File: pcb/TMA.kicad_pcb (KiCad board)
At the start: 2 copper layers, 6 parts, among them U1 BMP280, U2 BMI160, U3 STM32F030C6Tx

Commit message: Pick components.
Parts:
- added C4: 4u7, Capacitor_SMD:C_0402_1005Metric, F.Cu at (116.0, 84.4)
- added C5: 100nF, Capacitor_SMD:C_0402_1005Metric, F.Cu at (111.2, 88.7)
- added C6: 4u7, Capacitor_SMD:C_0402_1005Metric, F.Cu at (114.1, 86.4)
- added C7: 100nF, Capacitor_SMD:C_0402_1005Metric, F.Cu at (110.5, 90.7)
- added D1: D_Schottky, Diode_SMD:D_0402_1005Metric, F.Cu at (82.8, 91.9)
- added D3: BLUE, LED_SMD:LED_0402_1005Metric, F.Cu at (103.4, 75.9)
- added D4: RED, LED_SMD:LED_0402_1005Metric, F.Cu at (103.4, 80.0)
- added J1: Conn_01x02, Connector_JST:JST_PH_B2B-PH-K_1x02_P2.00mm_Vertical, F.Cu at (88.1, 64.5)
- added J2: Conn_01x06, Connector_JST:JST_PH_B6B-PH-K_1x06_P2.00mm_Vertical, F.Cu at (93.5, 63.5)
- added R1: 5k, Resistor_SMD:R_0402_1005Metric, F.Cu at (108.3, 86.7)
- added R2: 10k, Resistor_SMD:R_0402_1005Metric, F.Cu at (106.4, 75.9)
- added R3: 10k, Resistor_SMD:R_0402_1005Metric, F.Cu at (106.4, 80.0)
- added R4: 10k, Resistor_SMD:R_0402_1005Metric, F.Cu at (108.3, 88.7)
- added R5: 10k, Resistor_SMD:R_0402_1005Metric, F.Cu at (122.9, 82.0)
- added SW1: SW_SPDT, Button_Switch_SMD:SW_SPDT_PCM12, F.Cu at (86.4, 74.4)
- added U4: MIC5504-3.3YM5, Package_TO_SOT_SMD:SOT-23-5, F.Cu at (77.7, 93.0)
- U3: value STM32F030C6Tx -> ATtiny1614-SS; footprint Package_QFP:LQFP-48_7x7mm_P0.5mm -> Package_SO:SOIC-14_3.9x8.7mm_P1.27mm
- moved U1 37.4 mm to (107.4, 69.6)
- moved U3 36.9 mm to (96.0, 74.7)
- moved C3 31.0 mm to (107.7, 90.7)
- moved C2 30.3 mm to (122.7, 70.1)
- moved U2 30.0 mm to (114.0, 69.8)
- moved C1 24.6 mm to (114.1, 88.4)
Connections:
- U3 pad 10: Net-(U3-Pad10) -> UPDI
- U3 pad 11: Net-(U3-Pad11) -> SDA
- U3 pad 12: Net-(U3-Pad12) -> SCL
- U3 pad 14: Net-(U3-Pad14) -> GND
- U3 pad 6: Net-(U3-Pad6) -> MODE
- U3 pad 7: GND -> Net-(U3-Pad7)
- U3 pad 8: GND -> LED1
- U3 pad 9: +3V3 -> LED0
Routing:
- net GND: track 0.00 -> 4.32 mm
- net Net-(D3-Pad1): track 0.00 -> 2.08 mm
- net Net-(D4-Pad1): track 0.00 -> 2.05 mm

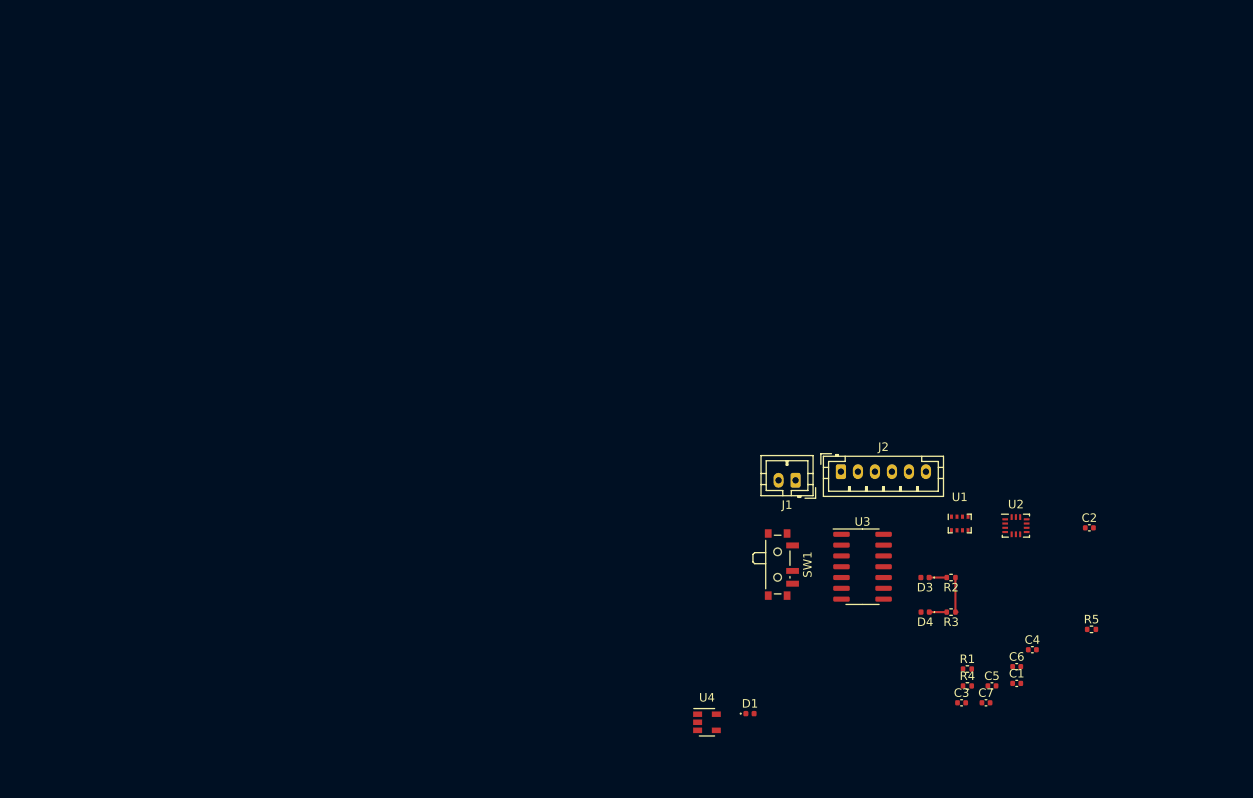
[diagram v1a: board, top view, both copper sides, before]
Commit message: Simplify, add voltage to extension.
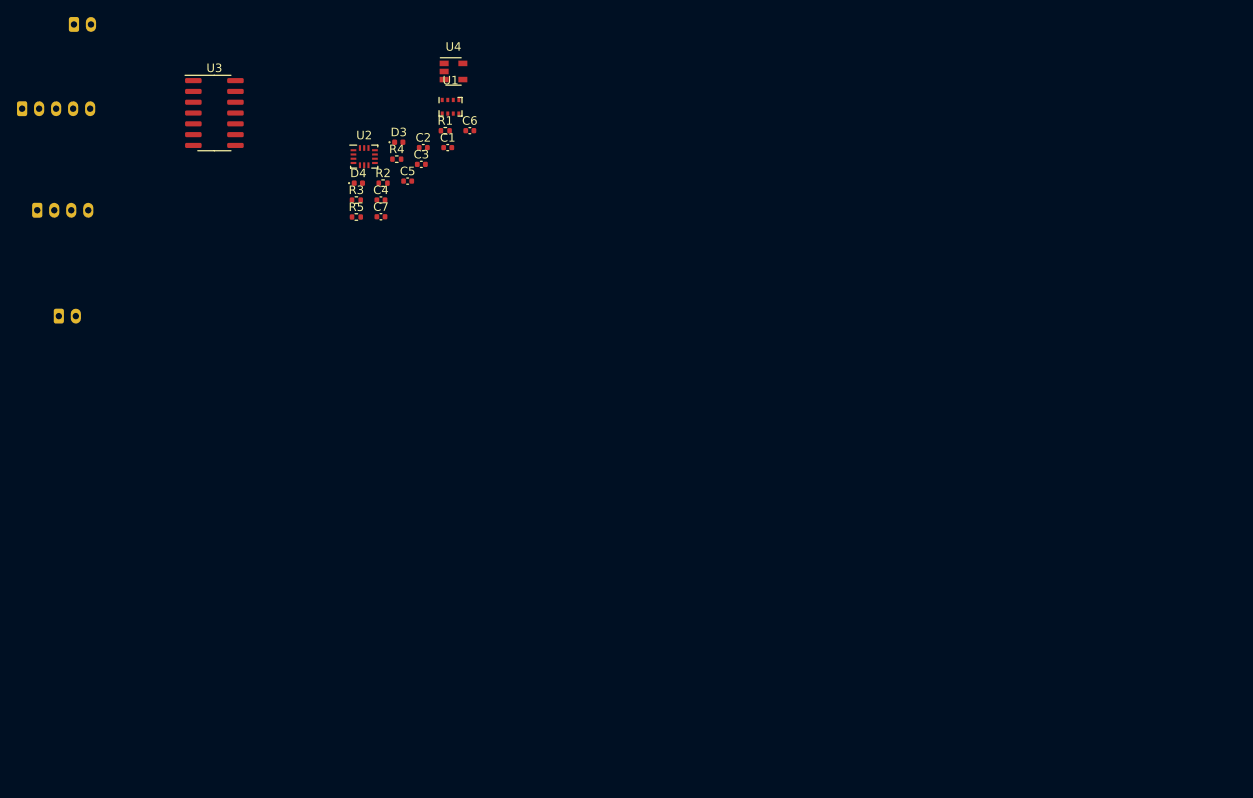
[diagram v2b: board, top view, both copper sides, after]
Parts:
- removed D1: D_Schottky, Diode_SMD:D_0402_1005Metric
- removed SW1: SW_SPDT, Button_Switch_SMD:SW_SPDT_PCM12
- added J3: Conn_01x04, Connector_JST:JST_PH_S4B-PH-K_1x04_P2.00mm_Horizontal, B.Cu at (-1.02, 32.8)
- added J4: Conn_01x02, Connector_JST:JST_PH_S2B-PH-K_1x02_P2.00mm_Horizontal, B.Cu at (3.30, 10.9)
- J1: footprint Connector_JST:JST_PH_B2B-PH-K_1x02_P2.00mm_Vertical -> Connector_JST:JST_PH_S2B-PH-K_1x02_P2.00mm_Horizontal; moved to B.Cu
- J2: value Conn_01x06 -> Conn_01x05; footprint Connector_JST:JST_PH_B6B-PH-K_1x06_P2.00mm_Vertical -> Connector_JST:JST_PH_S5B-PH-K_1x05_P2.00mm_Horizontal; moved to B.Cu
- R1: value 5k -> 10k
- R2, R3: value 10k -> 100
- R4, R5: value 10k -> 4k7
- moved J2 105.3 mm to (-2.79, 20.8)
- moved R5 99.1 mm to (36.5, 33.6)
- moved C4 93.1 mm to (39.4, 31.6)
- moved U3 93.0 mm to (19.8, 21.3)
- moved C1 91.9 mm to (47.2, 25.4)
- moved R4 91.3 mm to (41.3, 26.8)
- moved C7 91.2 mm to (39.4, 33.5)
- moved C5 90.8 mm to (42.5, 29.3)
- moved C2 90.2 mm to (44.4, 25.4)
- moved C6 90.0 mm to (49.8, 23.4)
- moved C3 89.7 mm to (44.1, 27.4)
- moved J1 88.7 mm to (1.52, 45.2), turned to 0 degrees
- moved R1 88.2 mm to (47.0, 23.4)
- moved U2 88.1 mm to (37.4, 26.5)
- moved R3 85.1 mm to (36.5, 31.6), turned to 0 degrees
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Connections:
- J2 pad 1: SCL -> TXD
- J2 pad 2: SDA -> RXD
- J2 pad 3: GND -> UPDI
- J2 pad 4: UPDI -> GND
- J2 pad 5: Net-(J2-Pad5) -> +3V3
- R1 pad 1: UPDI -> GND
- R1 pad 2: Net-(J2-Pad5) -> MODE
- U3 pad 5: Net-(U3-Pad5) -> MODE
- U3 pad 6: MODE -> RXD
- U3 pad 7: Net-(U3-Pad7) -> TXD
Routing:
- net GND: track 4.32 -> 0.00 mm
- net Net-(D3-Pad1): track 2.08 -> 0.00 mm
- net Net-(D4-Pad1): track 2.05 -> 0.00 mm

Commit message: Routing!
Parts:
- J1, J4: footprint Connector_JST:JST_PH_S2B-PH-K_1x02_P2.00mm_Horizontal -> Connector_PinHeader_1.00mm:PinHeader_1x02_P1.00mm_Vertical_SMD_Pin1Left
- J2: footprint Connector_JST:JST_PH_S5B-PH-K_1x05_P2.00mm_Horizontal -> Connector_PinHeader_1.00mm:PinHeader_1x05_P1.00mm_Vertical_SMD_Pin1Left
- J3: footprint Connector_JST:JST_PH_S4B-PH-K_1x04_P2.00mm_Horizontal -> Connector_PinHeader_1.00mm:PinHeader_1x04_P1.00mm_Vertical_SMD_Pin1Left
- R1: moved to B.Cu
- moved J4 84.2 mm to (77.5, 50.8)
- moved J3 78.0 mm to (73.9, 54.6)
- moved J2 77.9 mm to (69.3, 50.3)
- moved J1 73.4 mm to (74.9, 44.5), turned to 90 degrees
- moved U3 59.0 mm to (71.4, 50.0)
- moved D4 49.5 mm to (78.5, 56.1), turned to 90 degrees
- moved U2 47.7 mm to (80.3, 47.5), turned to 90 degrees
- moved R3 47.6 mm to (77.0, 56.6)
- moved U1 45.7 mm to (79.8, 53.1)
- moved C2 45.3 mm to (83.1, 49.0), turned to 90 degrees
- moved D3 43.5 mm to (71.6, 56.1), turned to 90 degrees
- moved R2 43.1 mm to (73.2, 56.6), turned to 180 degrees
- moved R5 43.0 mm to (76.2, 50.0), turned to 180 degrees
- moved R1 42.9 mm to (78.2, 52.8), turned to 90 degrees
- moved R4 41.3 mm to (76.2, 48.8), turned to 180 degrees
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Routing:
- net +3V3: track 0.00 -> 55.1 mm, vias 0 -> 3
- net GND: track 0.00 -> 34.3 mm, vias 0 -> 2
- net SCL: track 0.00 -> 31.5 mm, vias 0 -> 3
- net SDA: track 0.00 -> 27.3 mm, vias 0 -> 3
- net MODE: track 0.00 -> 10.4 mm, vias 0 -> 1
- net LED1: track 0.00 -> 5.94 mm
- net UPDI: track 0.00 -> 5.80 mm, vias 0 -> 1
- net Net-(C4-Pad1): track 0.00 -> 5.66 mm, vias 0 -> 1
- net TXD: track 0.00 -> 5.01 mm, vias 0 -> 1
- net LED0: track 0.00 -> 4.56 mm
- net RXD: track 0.00 -> 3.52 mm, vias 0 -> 1
- net Net-(D4-Pad1): track 0.00 -> 1.02 mm
- net Net-(D3-Pad1): track 0.00 -> 1.02 mm
- added copper zone on B.Cu, net GND
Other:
- board outline added: 18 x 18 mm
